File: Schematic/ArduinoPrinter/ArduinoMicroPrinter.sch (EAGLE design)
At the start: 8 parts, among them CON1 STEPPER, CON2 TPH, IC1 ULN2003AN, U1 74HC04_HEX_INVERTER

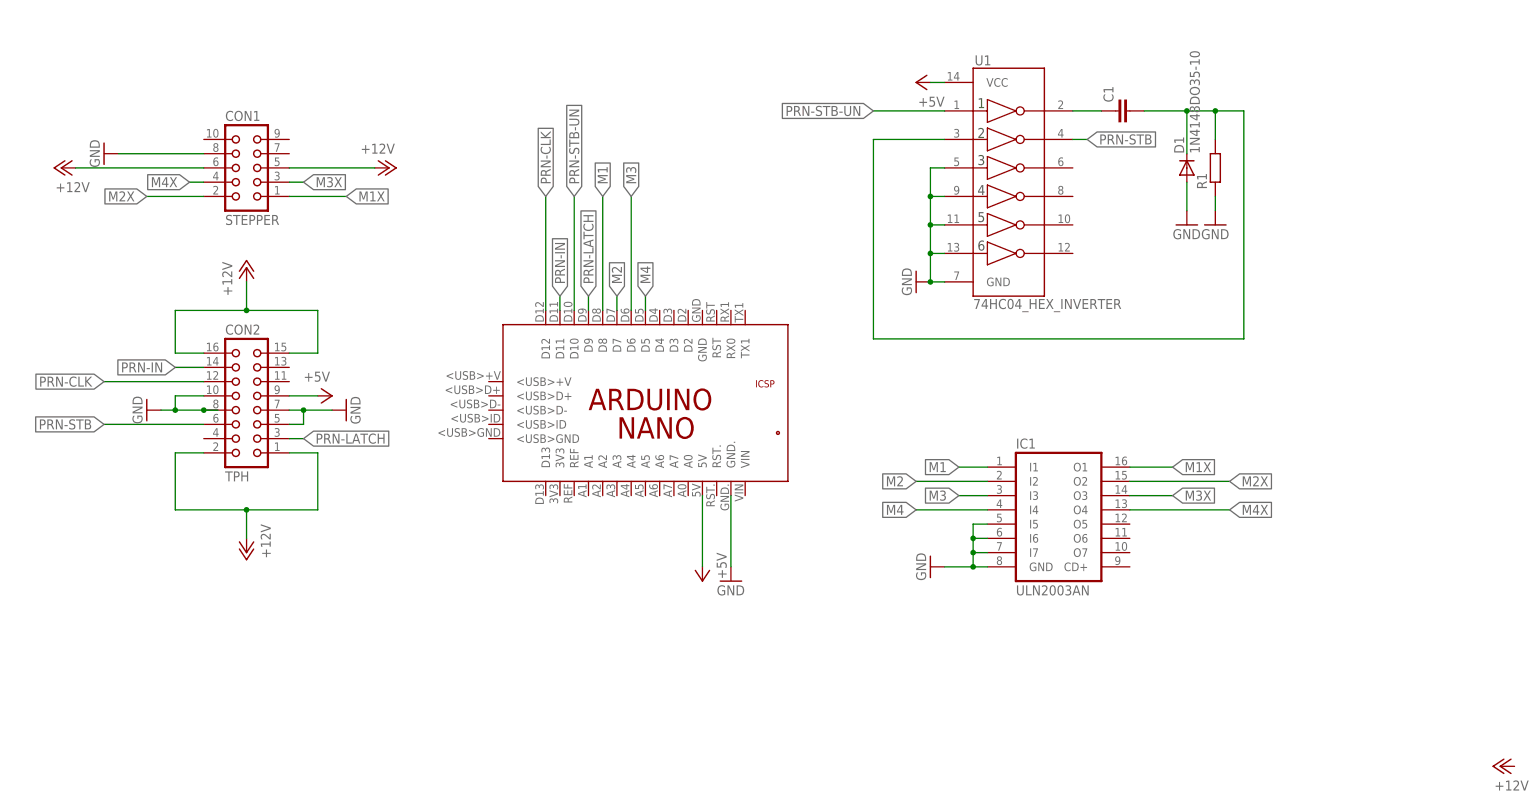
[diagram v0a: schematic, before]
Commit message: Added 12V power switch
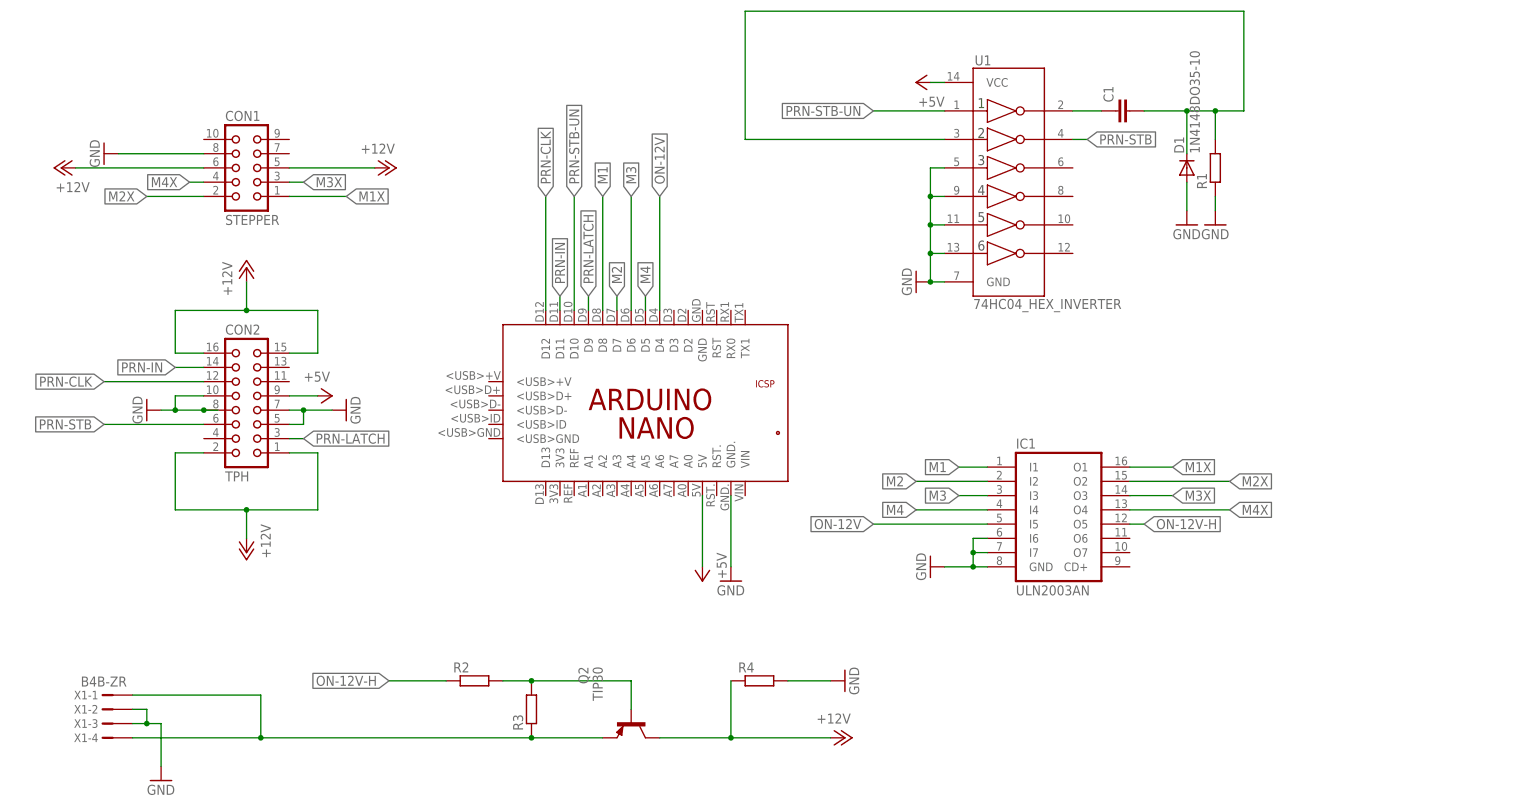
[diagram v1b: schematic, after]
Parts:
- added Q2: TIP30, transistor-pnp:TIP30
- added R2, R3, R4: (no value), resistor:R-EU_0207/12
- added X1: B4B-ZR, con-jst:B4B-ZR
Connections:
- new net N$3: Q2.B, R2.2, R3.2
- new net N$5: Q2.E, R3.1, X1-1.1, X1-4.1
- new net ON-12V: IC1.I5, PCB2.D4
- new net ON-12V-H: IC1.O5, R2.1
- net +12V: now also Q2.C, R4.1
- net GND: now also R4.2, X1-2.1, X1-3.1; no longer IC1.I5
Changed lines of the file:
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@@
 <part name="IC1" library="uln-udn" deviceset="ULN2003A" device="N"/>
 <part name="GND8" library="supply1" deviceset="GND" device=""/>
+<part name="Q2" library="transistor-pnp" deviceset="TIP30" device=""/>
+<part name="R2" library="resistor" deviceset="R-EU_" device="0207/12"/>
+<part name="R3" library="resistor" deviceset="R-EU_" device="0207/12"/>
+<part name="R4" library="resistor" deviceset="R-EU_" device="0207/12"/>
+<part name="GND9" library="supply1" deviceset="GND" device=""/>
+<part name="X1" library="con-jst" deviceset="?4B-ZR" device="B"/>
+<part name="GND10" library="supply1" deviceset="GND" device=""/>
 </parts>
 <sheets>
@@
 <instance part="P+4" gate="1" x="0" y="116.84" rot="R270"/>
 <instance part="P+5" gate="1" x="-58.42" y="116.84" rot="R90"/>
-<instance part="P+6" gate="1" x="198.12" y="10.16" rot="R90"/>
+<instance part="P+6" gate="1" x="81.28" y="15.24" rot="R270"/>
 <instance part="CON1" gate="G$1" x="-25.4" y="116.84"/>
 <instance part="CON2" gate="G$1" x="-25.4" y="76.2"/>
@@
 <instance part="IC1" gate="A" x="119.38" y="55.88"/>
 <instance part="GND8" gate="1" x="96.52" y="45.72" rot="R270"/>
+<instance part="Q2" gate="G$1" x="43.18" y="17.78" rot="MR270"/>
+<instance part="R2" gate="G$1" x="15.24" y="25.4"/>
+<instance part="R3" gate="G$1" x="25.4" y="20.32" rot="R90"/>
+<instance part="R4" gate="G$1" x="66.04" y="25.4"/>
+<instance part="GND9" gate="1" x="81.28" y="25.4" rot="R90"/>
+<instance part="X1" gate="-1" x="-50.8" y="22.86" rot="MR0"/>
+<instance part="X1" gate="-2" x="-50.8" y="20.32" rot="MR0"/>
+<instance part="X1" gate="-3" x="-50.8" y="17.78" rot="MR0"/>
+<instance part="X1" gate="-4" x="-50.8" y="15.24" rot="MR0"/>
+<instance part="GND10" gate="1" x="-40.64" y="7.62"/>
 </instances>
 <busses>
@@
 <pinref part="GND3" gate="1" pin="GND"/>
 <wire x1="99.06" y1="96.52" x2="96.52" y2="96.52" width="0.1524" layer="91"/>
-<pinref part="U1" gate="G$1" pin="3A"/>
-<wire x1="99.06" y1="116.84" x2="96.52" y2="116.84" width="0.1524" layer="91"/>
-<wire x1="96.52" y1="116.84" x2="96.52" y2="111.76" width="0.1524" layer="91"/>
 <junction x="96.52" y="96.52"/>
 <pinref part="U1" gate="G$1" pin="4A"/>
@@
 <wire x1="96.52" y1="101.6" x2="96.52" y2="96.52" width="0.1524" layer="91"/>
 <wire x1="99.06" y1="111.76" x2="96.52" y2="111.76" width="0.1524" layer="91"/>
-<junction x="96.52" y="111.76"/>
 <pinref part="U1" gate="G$1" pin="5A"/>
 <wire x1="99.06" y1="106.68" x2="96.52" y2="106.68" width="0.1524" layer="91"/>
@@
 <wire x1="99.06" y1="101.6" x2="96.52" y2="101.6" width="0.1524" layer="91"/>
 <junction x="96.52" y="101.6"/>
+<wire x1="96.52" y1="111.76" x2="96.52" y2="116.84" width="0.1524" layer="91"/>
+<junction x="96.52" y="111.76"/>
+<pinref part="U1" gate="G$1" pin="3A"/>
+<wire x1="96.52" y1="116.84" x2="99.06" y2="116.84" width="0.1524" layer="91"/>
 </segment>
 <segment>
@@
 <pinref part="IC1" gate="A" pin="GND"/>
 <wire x1="99.06" y1="45.72" x2="104.14" y2="45.72" width="0.1524" layer="91"/>
-<pinref part="IC1" gate="A" pin="I5"/>
 <wire x1="104.14" y1="45.72" x2="106.68" y2="45.72" width="0.1524" layer="91"/>
-<wire x1="106.68" y1="53.34" x2="104.14" y2="53.34" width="0.1524" layer="91"/>
-<wire x1="104.14" y1="53.34" x2="104.14" y2="50.8" width="0.1524" layer="91"/>
 <junction x="104.14" y="45.72"/>
 <pinref part="IC1" gate="A" pin="I6"/>
@@
 <wire x1="104.14" y1="48.26" x2="104.14" y2="45.72" width="0.1524" layer="91"/>
 <wire x1="106.68" y1="50.8" x2="104.14" y2="50.8" width="0.1524" layer="91"/>
-<junction x="104.14" y="50.8"/>
 <pinref part="IC1" gate="A" pin="I7"/>
 <wire x1="106.68" y1="48.26" x2="104.14" y2="48.26" width="0.1524" layer="91"/>
 <junction x="104.14" y="48.26"/>
+</segment>
+<segment>
+<pinref part="R4" gate="G$1" pin="2"/>
+<wire x1="71.12" y1="25.4" x2="78.74" y2="25.4" width="0.1524" layer="91"/>
+<pinref part="GND9" gate="1" pin="GND"/>
+</segment>
+<segment>
+<pinref part="GND10" gate="1" pin="GND"/>
+<wire x1="-40.64" y1="10.16" x2="-40.64" y2="17.78" width="0.1524" layer="91"/>
+<pinref part="X1" gate="-2" pin="1"/>
+<wire x1="-45.72" y1="20.32" x2="-43.18" y2="20.32" width="0.1524" layer="91"/>
+<wire x1="-43.18" y1="20.32" x2="-43.18" y2="17.78" width="0.1524" layer="91"/>
+<pinref part="X1" gate="-3" pin="1"/>
+<wire x1="-43.18" y1="17.78" x2="-45.72" y2="17.78" width="0.1524" layer="91"/>
+<wire x1="-40.64" y1="17.78" x2="-43.18" y2="17.78" width="0.1524" layer="91"/>
+<junction x="-43.18" y="17.78"/>
 </segment>
 </net>
@@
 <junction x="-25.4" y="55.88"/>
 </segment>
+<segment>
+<pinref part="Q2" gate="G$1" pin="C"/>
+<wire x1="48.26" y1="15.24" x2="60.96" y2="15.24" width="0.1524" layer="91"/>
+<pinref part="R4" gate="G$1" pin="1"/>
+<wire x1="60.96" y1="15.24" x2="78.74" y2="15.24" width="0.1524" layer="91"/>
+<wire x1="60.96" y1="25.4" x2="60.96" y2="15.24" width="0.1524" layer="91"/>
+<junction x="60.96" y="15.24"/>
+<pinref part="P+6" gate="1" pin="+12V"/>
+</segment>
 </net>
 <net name="PRN-LATCH" class="0">
@@
 <junction x="142.24" y="127"/>
 <wire x1="147.32" y1="127" x2="152.4" y2="127" width="0.1524" layer="91"/>
-<wire x1="152.4" y1="127" x2="152.4" y2="86.36" width="0.1524" layer="91"/>
+<wire x1="152.4" y1="127" x2="152.4" y2="144.78" width="0.1524" layer="91"/>
 <junction x="147.32" y="127"/>
-<wire x1="152.4" y1="86.36" x2="86.36" y2="86.36" width="0.1524" layer="91"/>
-<wire x1="86.36" y1="86.36" x2="86.36" y2="121.92" width="0.1524" layer="91"/>
+<wire x1="152.4" y1="144.78" x2="63.5" y2="144.78" width="0.1524" layer="91"/>
+<wire x1="63.5" y1="144.78" x2="63.5" y2="121.92" width="0.1524" layer="91"/>
 <pinref part="U1" gate="G$1" pin="2A"/>
-<wire x1="86.36" y1="121.92" x2="99.06" y2="121.92" width="0.1524" layer="91"/>
-</segment>
-</net>
+<wire x1="63.5" y1="121.92" x2="99.06" y2="121.92" width="0.1524" layer="91"/>
+</segment>
+</net>
+<net name="ON-12V" class="0">
+<segment>
+<pinref part="PCB2" gate="G$1" pin="D4"/>
+<wire x1="48.26" y1="91.44" x2="48.26" y2="111.76" width="0.1524" layer="91"/>
+<label x="48.26" y="111.76" size="1.778" layer="95" rot="R90" xref="yes"/>
+</segment>
+<segment>
+<label x="86.36" y="53.34" size="1.778" layer="95" rot="R180" xref="yes"/>
+<pinref part="IC1" gate="A" pin="I5"/>
+<wire x1="106.68" y1="53.34" x2="86.36" y2="53.34" width="0.1524" layer="91"/>
+</segment>
+</net>
+<net name="ON-12V-H" class="0">
+<segment>
+<pinref part="IC1" gate="A" pin="O5"/>
+<wire x1="132.08" y1="53.34" x2="134.62" y2="53.34" width="0.1524" layer="91"/>
+<label x="134.62" y="53.34" size="1.778" layer="95" xref="yes"/>
+</segment>
+<segment>
+<pinref part="R2" gate="G$1" pin="1"/>
+<wire x1="10.16" y1="25.4" x2="0" y2="25.4" width="0.1524" layer="91"/>
+<label x="0" y="25.4" size="1.778" layer="95" rot="R180" xref="yes"/>
+</segment>
+</net>
+<net name="N$3" class="0">
+<segment>
+<pinref part="R2" gate="G$1" pin="2"/>
+<pinref part="R3" gate="G$1" pin="2"/>
+<wire x1="20.32" y1="25.4" x2="25.4" y2="25.4" width="0.1524" layer="91"/>
+<pinref part="Q2" gate="G$1" pin="B"/>
+<wire x1="43.18" y1="20.32" x2="43.18" y2="25.4" width="0.1524" layer="91"/>
+<wire x1="43.18" y1="25.4" x2="25.4" y2="25.4" width="0.1524" layer="91"/>
+<junction x="25.4" y="25.4"/>
+</segment>
+</net>
+<net name="N$5" class="0">
+<segment>
+<pinref part="R3" gate="G$1" pin="1"/>
+<pinref part="Q2" gate="G$1" pin="E"/>
+<wire x1="25.4" y1="15.24" x2="38.1" y2="15.24" width="0.1524" layer="91"/>
+<junction x="25.4" y="15.24"/>
+<pinref part="X1" gate="-4" pin="1"/>
+<wire x1="-45.72" y1="15.24" x2="-22.86" y2="15.24" width="0.1524" layer="91"/>
+<pinref part="X1" gate="-1" pin="1"/>
+<wire x1="-22.86" y1="15.24" x2="25.4" y2="15.24" width="0.1524" layer="91"/>
+<wire x1="-45.72" y1="22.86" x2="-22.86" y2="22.86" width="0.1524" layer="91"/>
+<wire x1="-22.86" y1="22.86" x2="-22.86" y2="15.24" width="0.1524" layer="91"/>
+<junction x="-22.86" y="15.24"/>
+</segment>
+</net>

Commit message: Supports of a text printing. There one problem: lack of a good font and font experience.
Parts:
- C1: value (none) -> 1000n
- D1: value 1N4148DO35-10 -> КД522Б
- IC1: value ULN2003AN -> ULN2003A
- R1: value (none) -> 2k; device resistor:R-EU_0309/12 -> resistor:R-EU_0207/12
- R2: value (none) -> 2k
- R3: value (none) -> 6.8k
- R4: value (none) -> 100k; device resistor:R-EU_0207/12 -> resistor:R-EU_0309/12
- U1: value 74HC04_HEX_INVERTER -> 74HC04
- VT1: value TIP30 -> КТ853Г
- renumbered PCB2 to PCB1, Q2 to VT1
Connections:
- net +12V: now also R3.1; no longer R4.1
- net GND: now also R3.2, R4.1; no longer R1.1, R4.2
- net N$2: now also R4.2; no longer R1.2
- net N$3: now also R1.2; no longer R3.2
- net N$5: now also R2.1; no longer R3.1
- net ON-12V-H: now also R1.1; no longer R2.1
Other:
- moved on the sheet: D1, R1, R2, R3, R4
